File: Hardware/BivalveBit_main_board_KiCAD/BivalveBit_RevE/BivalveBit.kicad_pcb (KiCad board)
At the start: 2 copper layers, 89.9 x 17.8 mm, 58 parts, among them J2 Conn_01x01_Male, J4 Conn_01x01_Male, J5 Conn_01x01_Male, J6 Conn_01x03_Male, J7 Conn_01x01_Male, J8 Conn_01x01_Male, Q1 BSS138, Q2 BSS138, Q3 P-FET, SW2 SW_Reed, U2 ATmega4808-A, U3 LP5907MFX-3.0, U4 BJT_NPN

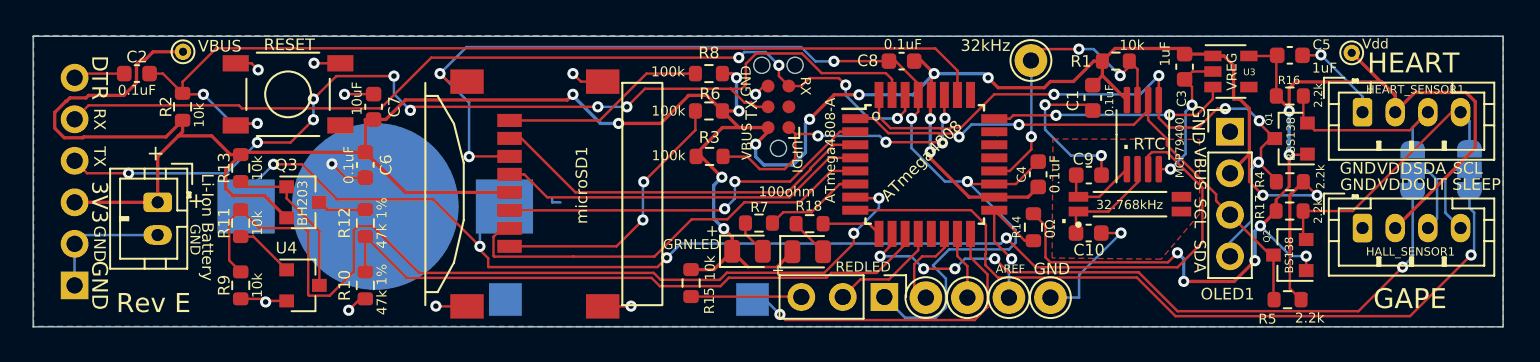
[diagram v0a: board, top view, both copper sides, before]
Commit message: Thickening traces, no layout changes
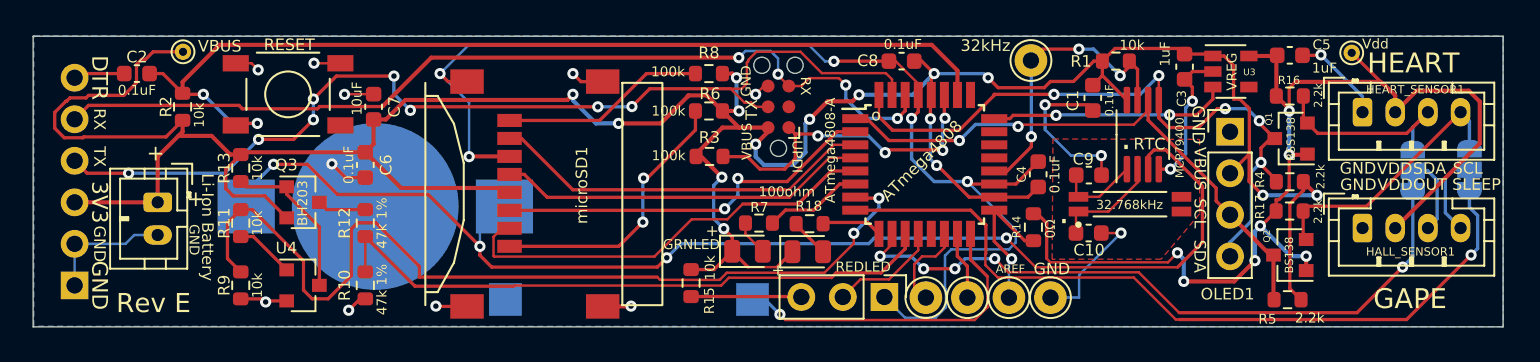
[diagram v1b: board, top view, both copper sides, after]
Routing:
- net VBUS: track 190.5 -> 189.1 mm
- net +BATT: track 77.9 -> 76.8 mm
- net GND: track 132.0 -> 131.0 mm
- net /BATT_MON_EN: track 57.4 -> 56.5 mm
- net /UPDI: track 19.6 -> 20.4 mm
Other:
- board text added: "BivalveBit RevE 2023 luke.miller@sdsu.edu"
- board text removed: "BivalveBit RevE 2021 luke.miller@sdsu.edu"
